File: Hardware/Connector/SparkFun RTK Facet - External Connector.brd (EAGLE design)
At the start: 54 x 22 mm, 40 parts, among them J1 FPC_12_0.5MM_BACKFLIP, J4 Qwiic, J5 u-blox USB, J6 FPC_12_0.5MM_BACKFLIP

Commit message: Update silk
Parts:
- removed U$10: (no value), output:RTK_SURVEYOR0
- added U$13, U$3: (no value), output:RTK5#SVG0
- added U$14: (no value), output:RTK_FACET0
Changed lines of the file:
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@@
 <layer number="45" name="Holes" color="7" fill="1" visible="yes" active="yes"/>
 <layer number="46" name="Milling" color="3" fill="1" visible="no" active="yes"/>
-<layer number="47" name="Measures" color="7" fill="1" visible="yes" active="yes"/>
+<layer number="47" name="Measures" color="7" fill="1" visible="no" active="yes"/>
 <layer number="48" name="Document" color="7" fill="1" visible="no" active="yes"/>
 <layer number="49" name="Reference" color="7" fill="1" visible="no" active="yes"/>
@@
 <element name="U$2" library="output" package="CONNECTORS1" value="" x="22" y="12" smashed="yes" rot="MR0"/>
 <element name="U$9" library="output" package="EXTERNAL0" value="" x="30" y="12" smashed="yes" rot="MR0"/>
-<element name="U$10" library="output" package="RTK_SURVEYOR0" value="" x="25" y="14" smashed="yes" rot="MR0"/>
 <element name="LOGO3" library="SparkFun-Aesthetics" package="QWIIC_5.5MM" value="QWIIC_LOGO_CONNECTOR" x="33" y="7" smashed="yes"/>
 <element name="U$8" library="output" package="EC10" value="" x="45" y="14" smashed="yes"/>
@@
 <attribute name="PROD_ID" value="CONN-15766" x="36" y="17" size="1.778" layer="27" rot="R180" display="off"/>
 </element>
+<element name="U$3" library="output" package="RTK5#SVG0" value="" x="27" y="15" smashed="yes"/>
+<element name="U$13" library="output" package="RTK5#SVG0" value="" x="27" y="5" smashed="yes" rot="MR0"/>
+<element name="U$14" library="output" package="RTK_FACET0" value="" x="26.4" y="14.3" smashed="yes" rot="MR0"/>
 </elements>
 <signals>

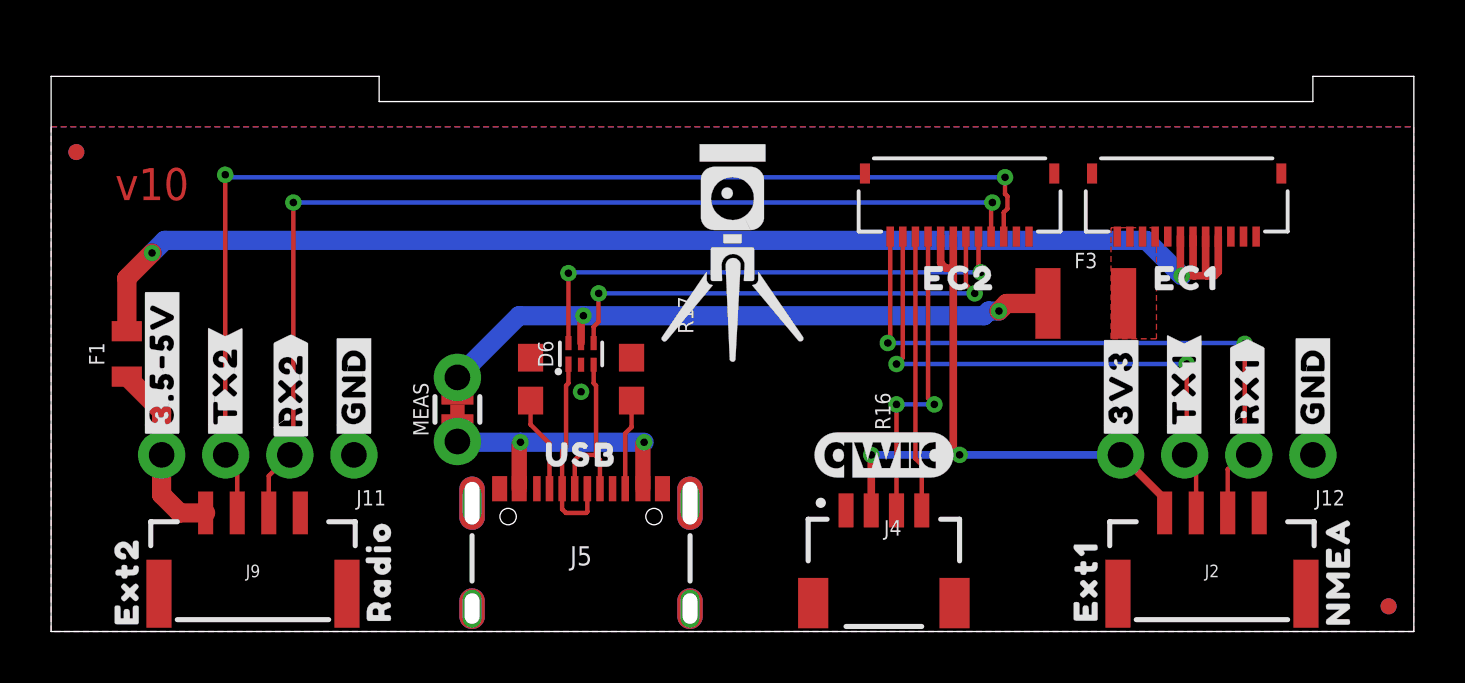
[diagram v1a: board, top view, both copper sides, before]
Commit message: Increase external connector board height to 23mm.
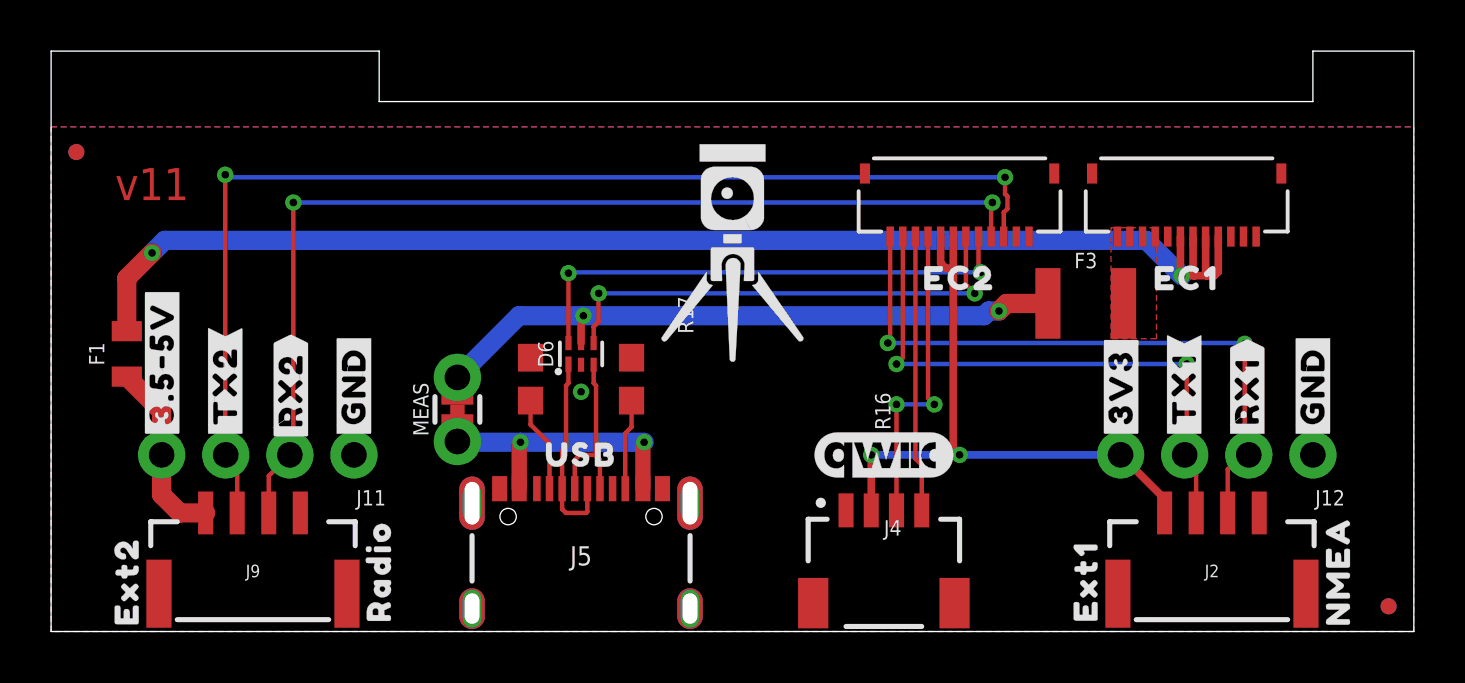
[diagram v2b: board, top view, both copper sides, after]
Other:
- board size 54 x 22 mm -> 54 x 23 mm
- board text added: "v11"
- board text removed: "v10"
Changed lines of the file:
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@@
 <layer number="23" name="tOrigins" color="15" fill="1" visible="yes" active="yes"/>
 <layer number="24" name="bOrigins" color="15" fill="1" visible="yes" active="yes"/>
-<layer number="25" name="tNames" color="7" fill="1" visible="no" active="yes"/>
-<layer number="26" name="bNames" color="7" fill="1" visible="no" active="yes"/>
-<layer number="27" name="tValues" color="7" fill="1" visible="no" active="yes"/>
-<layer number="28" name="bValues" color="7" fill="1" visible="no" active="yes"/>
-<layer number="29" name="tStop" color="7" fill="3" visible="no" active="yes"/>
-<layer number="30" name="bStop" color="7" fill="6" visible="no" active="yes"/>
-<layer number="31" name="tCream" color="7" fill="4" visible="no" active="yes"/>
-<layer number="32" name="bCream" color="7" fill="5" visible="no" active="yes"/>
-<layer number="33" name="tFinish" color="6" fill="3" visible="no" active="yes"/>
-<layer number="34" name="bFinish" color="6" fill="6" visible="no" active="yes"/>
-<layer number="35" name="tGlue" color="7" fill="4" visible="no" active="yes"/>
-<layer number="36" name="bGlue" color="7" fill="5" visible="no" active="yes"/>
-<layer number="37" name="tTest" color="7" fill="1" visible="no" active="yes"/>
-<layer number="38" name="bTest" color="7" fill="1" visible="no" active="yes"/>
-<layer number="39" name="tKeepout" color="4" fill="11" visible="no" active="yes"/>
-<layer number="40" name="bKeepout" color="1" fill="11" visible="no" active="yes"/>
-<layer number="41" name="tRestrict" color="4" fill="10" visible="no" active="yes"/>
-<layer number="42" name="bRestrict" color="1" fill="10" visible="no" active="yes"/>
-<layer number="43" name="vRestrict" color="2" fill="10" visible="no" active="yes"/>
-<layer number="44" name="Drills" color="7" fill="1" visible="no" active="yes"/>
+<layer number="25" name="tNames" color="7" fill="1" visible="yes" active="yes"/>
+<layer number="26" name="bNames" color="7" fill="1" visible="yes" active="yes"/>
+<layer number="27" name="tValues" color="7" fill="1" visible="yes" active="yes"/>
+<layer number="28" name="bValues" color="7" fill="1" visible="yes" active="yes"/>
+<layer number="29" name="tStop" color="7" fill="3" visible="yes" active="yes"/>
+<layer number="30" name="bStop" color="7" fill="6" visible="yes" active="yes"/>
+<layer number="31" name="tCream" color="7" fill="4" visible="yes" active="yes"/>
+<layer number="32" name="bCream" color="7" fill="5" visible="yes" active="yes"/>
+<layer number="33" name="tFinish" color="6" fill="3" visible="yes" active="yes"/>
+<layer number="34" name="bFinish" color="6" fill="6" visible="yes" active="yes"/>
+<layer number="35" name="tGlue" color="7" fill="4" visible="yes" active="yes"/>
+<layer number="36" name="bGlue" color="7" fill="5" visible="yes" active="yes"/>
+<layer number="37" name="tTest" color="7" fill="1" visible="yes" active="yes"/>
+<layer number="38" name="bTest" color="7" fill="1" visible="yes" active="yes"/>
+<layer number="39" name="tKeepout" color="4" fill="11" visible="yes" active="yes"/>
+<layer number="40" name="bKeepout" color="1" fill="11" visible="yes" active="yes"/>
+<layer number="41" name="tRestrict" color="4" fill="10" visible="yes" active="yes"/>
+<layer number="42" name="bRestrict" color="1" fill="10" visible="yes" active="yes"/>
+<layer number="43" name="vRestrict" color="2" fill="10" visible="yes" active="yes"/>
+<layer number="44" name="Drills" color="7" fill="1" visible="yes" active="yes"/>
 <layer number="45" name="Holes" color="7" fill="1" visible="yes" active="yes"/>
-<layer number="46" name="Milling" color="3" fill="1" visible="no" active="yes"/>
-<layer number="47" name="Measures" color="7" fill="1" visible="no" active="yes"/>
-<layer number="48" name="Document" color="7" fill="1" visible="no" active="yes"/>
-<layer number="49" name="Reference" color="7" fill="1" visible="no" active="yes"/>
-<layer number="50" name="dxf" color="7" fill="1" visible="no" active="yes"/>
+<layer number="46" name="Milling" color="3" fill="1" visible="yes" active="yes"/>
+<layer number="47" name="Measures" color="7" fill="1" visible="yes" active="yes"/>
+<layer number="48" name="Document" color="7" fill="1" visible="yes" active="yes"/>
+<layer number="49" name="Reference" color="7" fill="1" visible="yes" active="yes"/>
+<layer number="50" name="dxf" color="7" fill="1" visible="yes" active="yes"/>
 <layer number="51" name="tDocu" color="6" fill="1" visible="yes" active="yes"/>
-<layer number="52" name="bDocu" color="7" fill="1" visible="no" active="yes"/>
+<layer number="52" name="bDocu" color="7" fill="1" visible="yes" active="yes"/>
 <layer number="2" name="Horz/GND" color="1" fill="3" visible="no" active="no"/>
 <layer number="15" name="Vert" color="4" fill="6" visible="no" active="no"/>
@@
 <board>
 <plain>
-<text x="4" y="17.73" size="1.27" layer="1" font="vector" ratio="15" rot="SR0" align="center">v10</text>
+<text x="4" y="17.73" size="1.27" layer="1" font="vector" ratio="15" rot="SR0" align="center">v11</text>
 <text x="58.42" y="15.24" size="1.27" layer="51" font="vector" ratio="15">Board thickness is 1.6mm</text>
-<wire x1="54" y1="22" x2="54" y2="0" width="0.05" layer="20"/>
+<wire x1="54" y1="23" x2="54" y2="0" width="0.05" layer="20"/>
 <wire x1="54" y1="0" x2="0" y2="0" width="0.05" layer="20"/>
-<wire x1="0" y1="0" x2="0" y2="22" width="0.05" layer="20"/>
+<wire x1="0" y1="0" x2="0" y2="23" width="0.05" layer="20"/>
 <rectangle x1="0" y1="0" x2="2" y2="20" layer="39"/>
 <rectangle x1="48" y1="0" x2="50" y2="20" layer="40"/>
@@
 <dimension x1="21" y1="0" x2="8" y2="0" x3="14.5" y3="-2" textsize="0.5" textratio="15" layer="47" width="0.05"/>
 <dimension x1="46" y1="0" x2="33" y2="0" x3="39.5" y3="-2" textsize="0.5" textratio="15" layer="47" width="0.05"/>
-<wire x1="54" y1="22" x2="50" y2="22" width="0.05" layer="20"/>
-<wire x1="50" y1="22" x2="50" y2="21" width="0.05" layer="20"/>
+<wire x1="54" y1="23" x2="50" y2="23" width="0.05" layer="20"/>
+<wire x1="50" y1="23" x2="50" y2="21" width="0.05" layer="20"/>
 <wire x1="50" y1="21" x2="13" y2="21" width="0.05" layer="20"/>
-<wire x1="13" y1="21" x2="13" y2="22" width="0.05" layer="20"/>
-<wire x1="13" y1="22" x2="0" y2="22" width="0.05" layer="20"/>
-<dimension x1="0" y1="0" x2="0" y2="22" x3="-3" y3="11" textsize="1" textratio="15" layer="47" width="0.1"/>
+<wire x1="13" y1="21" x2="13" y2="23" width="0.05" layer="20"/>
+<wire x1="13" y1="23" x2="0" y2="23" width="0.05" layer="20"/>
+<dimension x1="0" y1="0" x2="0" y2="23" x3="-3" y3="11.5" textsize="1" textratio="15" layer="47" width="0.1"/>
 <dimension x1="0" y1="22" x2="54" y2="22" x3="27" y3="27" textsize="1" textratio="15" layer="47" width="0.1"/>
 </plain>
@@
 <contactref element="J6" pad="2"/>
 <via x="21" y="9.5" extent="1-16" drill="0.3"/>
-<wire x1="47.25" y1="15.65" x2="47.75" y2="15.65" width="0" layer="19" extent="1-1"/>
-<wire x1="46.75" y1="15.65" x2="47.25" y2="15.65" width="0" layer="19" extent="1-1"/>
-<wire x1="38.75" y1="15.65" x2="46.75" y2="15.65" width="0" layer="19" extent="1-1"/>
-<wire x1="38.25" y1="15.65" x2="38.75" y2="15.65" width="0" layer="19" extent="1-1"/>
-<wire x1="50" y1="7" x2="47.75" y2="15.65" width="0" layer="19" extent="1-1"/>
-<wire x1="47.875" y1="4.7" x2="50" y2="7" width="0" layer="19" extent="1-1"/>
-<wire x1="31.5" y1="4.8" x2="38.25" y2="15.65" width="0" layer="19" extent="1-1"/>
-<wire x1="25.318" y1="5.085" x2="31.5" y2="4.8" width="0" layer="19" extent="1-1"/>
-<wire x1="24.225" y1="5.66" x2="25.318" y2="5.085" width="0" layer="19" extent="1-1"/>
-<wire x1="25.318" y1="0.905" x2="25.318" y2="5.085" width="0" layer="19" extent="1-1"/>
-<wire x1="21" y1="9.5" x2="24.225" y2="5.66" width="0" layer="19" extent="1-1"/>
-<wire x1="21" y1="10.57" x2="21" y2="9.5" width="0" layer="19" extent="1-1"/>
-<wire x1="23" y1="10.85" x2="21" y2="10.57" width="0" layer="19" extent="1-1"/>
-<wire x1="19" y1="10.85" x2="21" y2="10.57" width="0" layer="19" extent="1-1"/>
-<wire x1="17.775" y1="5.66" x2="21" y2="9.5" width="0" layer="19" extent="1-1"/>
-<wire x1="16.682" y1="5.085" x2="17.775" y2="5.66" width="0" layer="19" extent="1-1"/>
-<wire x1="16.682" y1="0.905" x2="16.682" y2="5.085" width="0" layer="19" extent="1-1"/>
-<wire x1="12" y1="7" x2="16.682" y2="5.085" width="0" layer="19" extent="1-1"/>
-<wire x1="9.875" y1="4.7" x2="12" y2="7" width="0" layer="19" extent="1-1"/>
 </signal>
 <signal name="ESP_22/SCL">
@@
 <vertex x="42" y="11.6"/>
 </polygon>
-<wire x1="43.25" y1="15.65" x2="43.75" y2="15.65" width="0" layer="19" extent="1-1"/>
-<wire x1="42.75" y1="15.65" x2="43.25" y2="15.65" width="0" layer="19" extent="1-1"/>
-<wire x1="42.25" y1="15.65" x2="42.75" y2="15.65" width="0" layer="19" extent="1-1"/>
-<wire x1="42.5" y1="13" x2="42.75" y2="15.65" width="0" layer="19" extent="1-1"/>
 </signal>
 <signal name="VIN1" class="1">

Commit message: Reduce Main, Connector, Display, and Cell board widths by 1mm to allow for v-score protrusion.
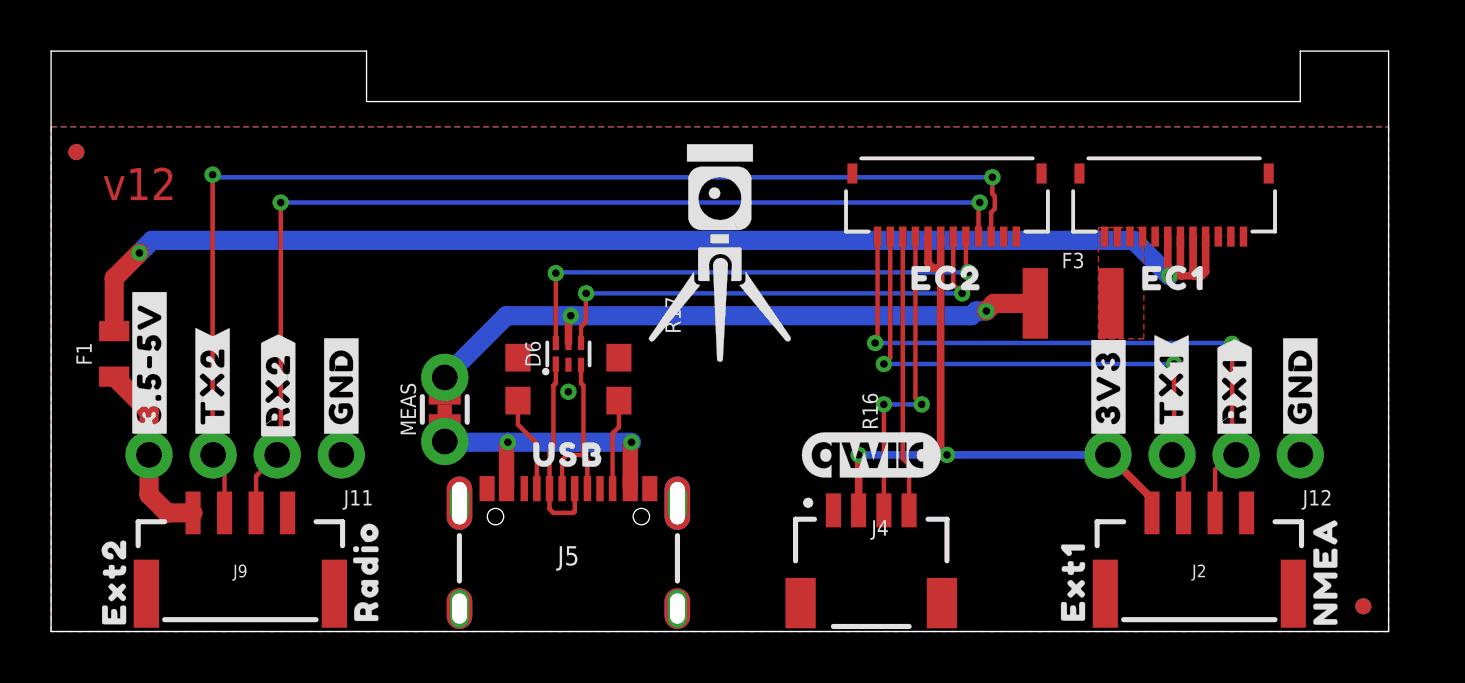
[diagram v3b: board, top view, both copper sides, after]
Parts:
- moved JP21 1.00 mm to (52.0, 1.00)
- moved JP71 1.00 mm to (52.0, 1.00)
- moved MEAS 0.50 mm to (15.6, 8.80)
- moved U$23 0.50 mm to (3.90, 7.50)
- moved D6 0.50 mm to (20.5, 11.0)
- moved F1 0.50 mm to (2.50, 11.0)
- moved F3 0.50 mm to (40.5, 13.0)
- moved J1 0.50 mm to (44.5, 17.0)
- moved J11 0.50 mm to (11.5, 7.00)
- moved J12 0.50 mm to (49.5, 7.00)
- moved J2 0.50 mm to (45.5, 1.40)
- moved J4 0.50 mm to (32.5, 4.80)
- moved J5 0.50 mm to (20.5, 6.00)
- moved J6 0.50 mm to (35.5, 17.0)
- moved J9 0.50 mm to (7.50, 1.40)
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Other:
- board size 54 x 23 mm -> 53 x 23 mm
- board text added: "v12"
- board text removed: "v11"
